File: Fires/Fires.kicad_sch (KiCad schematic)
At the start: 11 parts, among them J1 PowerSocket

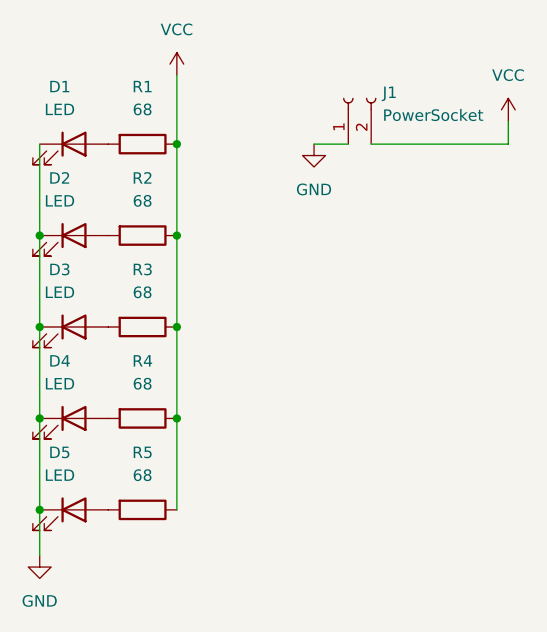
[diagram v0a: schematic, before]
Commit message: 出力を追加
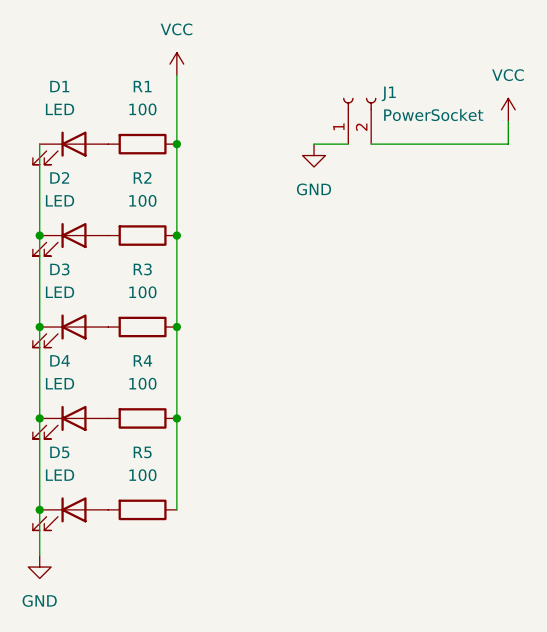
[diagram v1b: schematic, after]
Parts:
- R1, R2, R3, R4, R5: value 68 -> 100; footprint Resistor_THT:R_Axial_DIN0207_L6.3mm_D2.5mm_P10.16mm_Horizontal -> Resistor_SMD:R_0603_1608Metric
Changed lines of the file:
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@@
 			)
 		)
-		(property "Value" "68"
+		(property "Value" "100"
 			(at 138.43 130.81 90)
 			(effects
@@
 			)
 		)
-		(property "Footprint" "Resistor_THT:R_Axial_DIN0207_L6.3mm_D2.5mm_P10.16mm_Horizontal"
+		(property "Footprint" "Resistor_SMD:R_0603_1608Metric"
 			(at 138.43 132.842 90)
 			(effects
@@
 			)
 		)
-		(property "Value" "68"
+		(property "Value" "100"
 			(at 138.43 100.33 90)
 			(effects
@@
 			)
 		)
-		(property "Footprint" "Resistor_THT:R_Axial_DIN0207_L6.3mm_D2.5mm_P10.16mm_Horizontal"
+		(property "Footprint" "Resistor_SMD:R_0603_1608Metric"
 			(at 138.43 102.362 90)
 			(effects
@@
 			)
 		)
-		(property "Value" "68"
+		(property "Value" "100"
 			(at 138.43 110.49 90)
 			(effects
@@
 			)
 		)
-		(property "Footprint" "Resistor_THT:R_Axial_DIN0207_L6.3mm_D2.5mm_P10.16mm_Horizontal"
+		(property "Footprint" "Resistor_SMD:R_0603_1608Metric"
 			(at 138.43 112.522 90)
 			(effects
@@
 			)
 		)
-		(property "Value" "68"
+		(property "Value" "100"
 			(at 138.43 120.65 90)
 			(effects
@@
 			)
 		)
-		(property "Footprint" "Resistor_THT:R_Axial_DIN0207_L6.3mm_D2.5mm_P10.16mm_Horizontal"
+		(property "Footprint" "Resistor_SMD:R_0603_1608Metric"
 			(at 138.43 122.682 90)
 			(effects
@@
 			)
 		)
-		(property "Value" "68"
+		(property "Value" "100"
 			(at 138.43 90.17 90)
 			(effects
@@
 			)
 		)
-		(property "Footprint" "Resistor_THT:R_Axial_DIN0207_L6.3mm_D2.5mm_P10.16mm_Horizontal"
+		(property "Footprint" "Resistor_SMD:R_0603_1608Metric"
 			(at 138.43 92.202 90)
 			(effects
